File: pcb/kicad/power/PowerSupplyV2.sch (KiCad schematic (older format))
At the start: 61 parts, among them J1 12VWallWartVin, J2 AudioInput, J3 BackUpPower12V, J4 Display5V, J5 120Vinput, J7 Uc3.3VSignal, J8 Ucontroller3.3, U1 LM386, U11 BoostConv, U2 MOC3043M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

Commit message: Tile uC and antenna boards
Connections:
- wire segments 135 -> 141
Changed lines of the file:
@@
 	1    0    0    -1
 $EndComp
+Wire Wire Line
+	9750 4400 9750 4050
+Text Label 10200 3950 0    60   ~ 0
+5Voutput
 $Comp
 L CP C5
@@
 $EndComp
 Wire Wire Line
-	8900 3700 7950 3700
-Connection ~ 7950 3700
-Wire Wire Line
-	8450 3850 8450 3700
-Connection ~ 8450 3700
-Wire Wire Line
-	8750 3850 8750 3700
-Connection ~ 8750 3700
+	3350 2700 3350 2950
+Wire Wire Line
+	4800 2700 4800 3000
+Wire Wire Line
+	4250 3450 5500 3450
+Wire Wire Line
+	4800 3450 4800 3300
+Connection ~ 4800 3450
+Wire Wire Line
+	2700 3450 3950 3450
+Wire Wire Line
+	3350 3450 3350 3150
+Wire Wire Line
+	5050 3250 4950 3250
+Wire Wire Line
+	5350 3250 5500 3250
+Text Label 4850 2950 0    60   ~ 0
+MT2
+Text Label 4850 3400 0    60   ~ 0
+MT1
+Text Label 3350 2600 0    60   ~ 0
+ACLOAD
+Text Label 3300 3600 0    60   ~ 0
+ACNEUTRAL
 $Comp
 L R R12

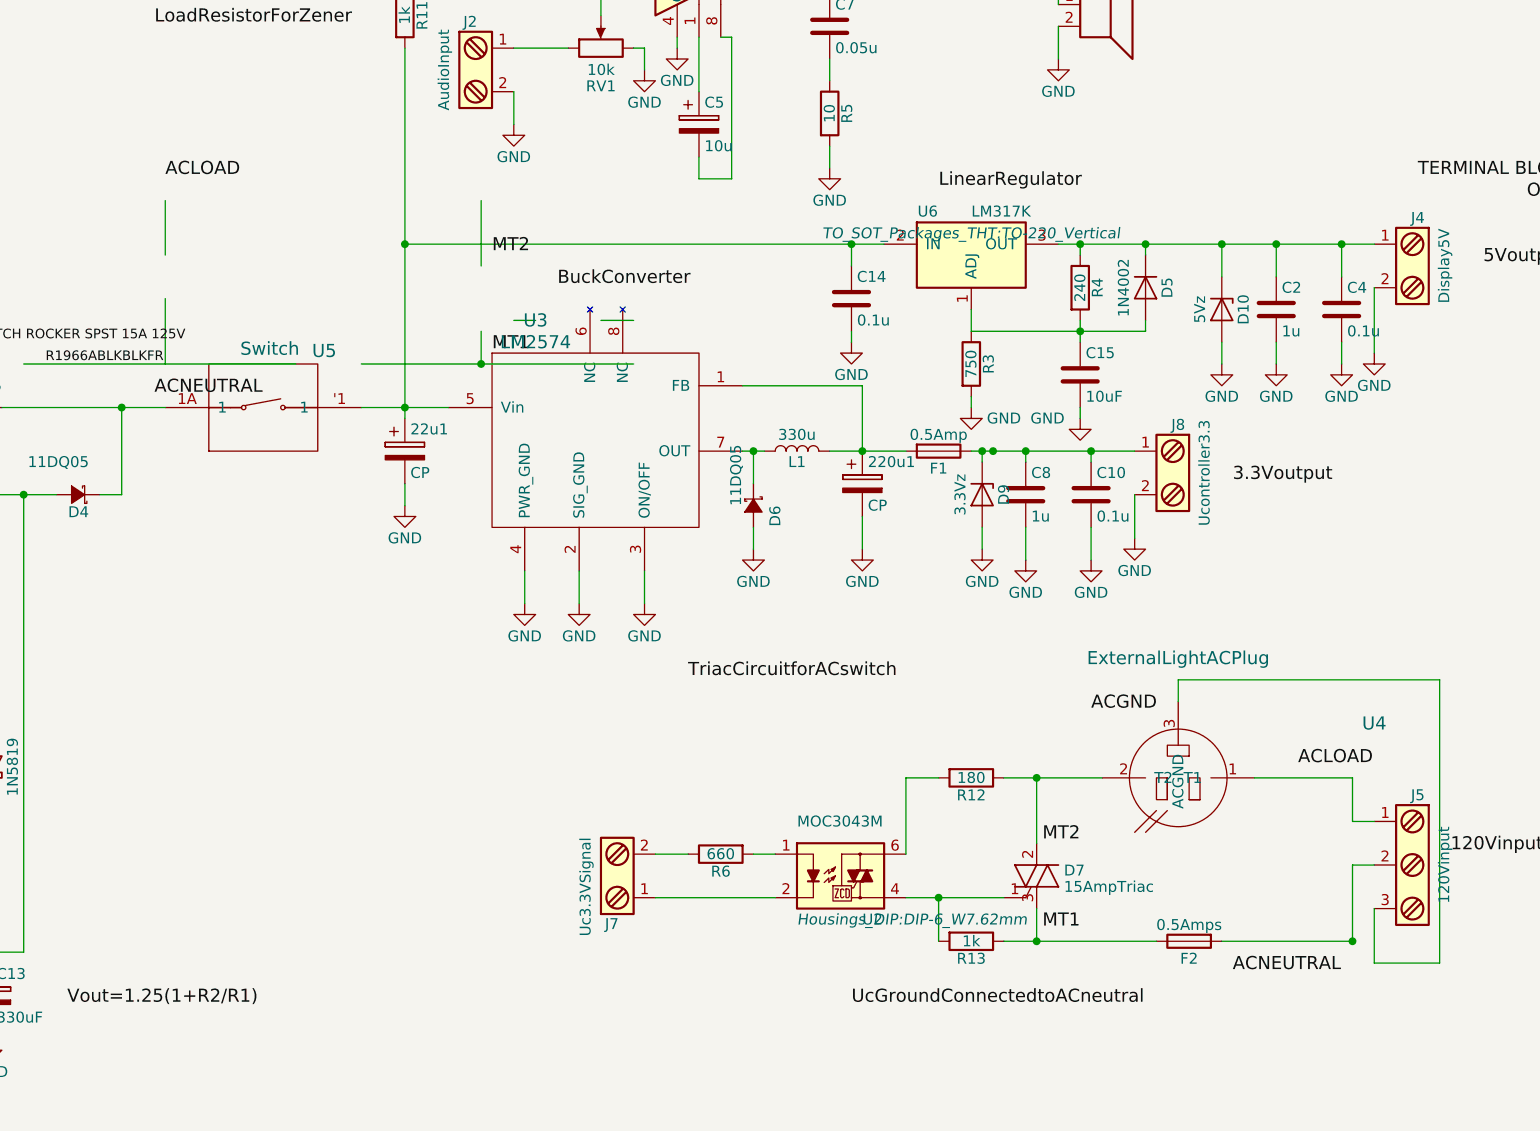
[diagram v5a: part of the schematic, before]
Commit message: Finish new base station and tile boards
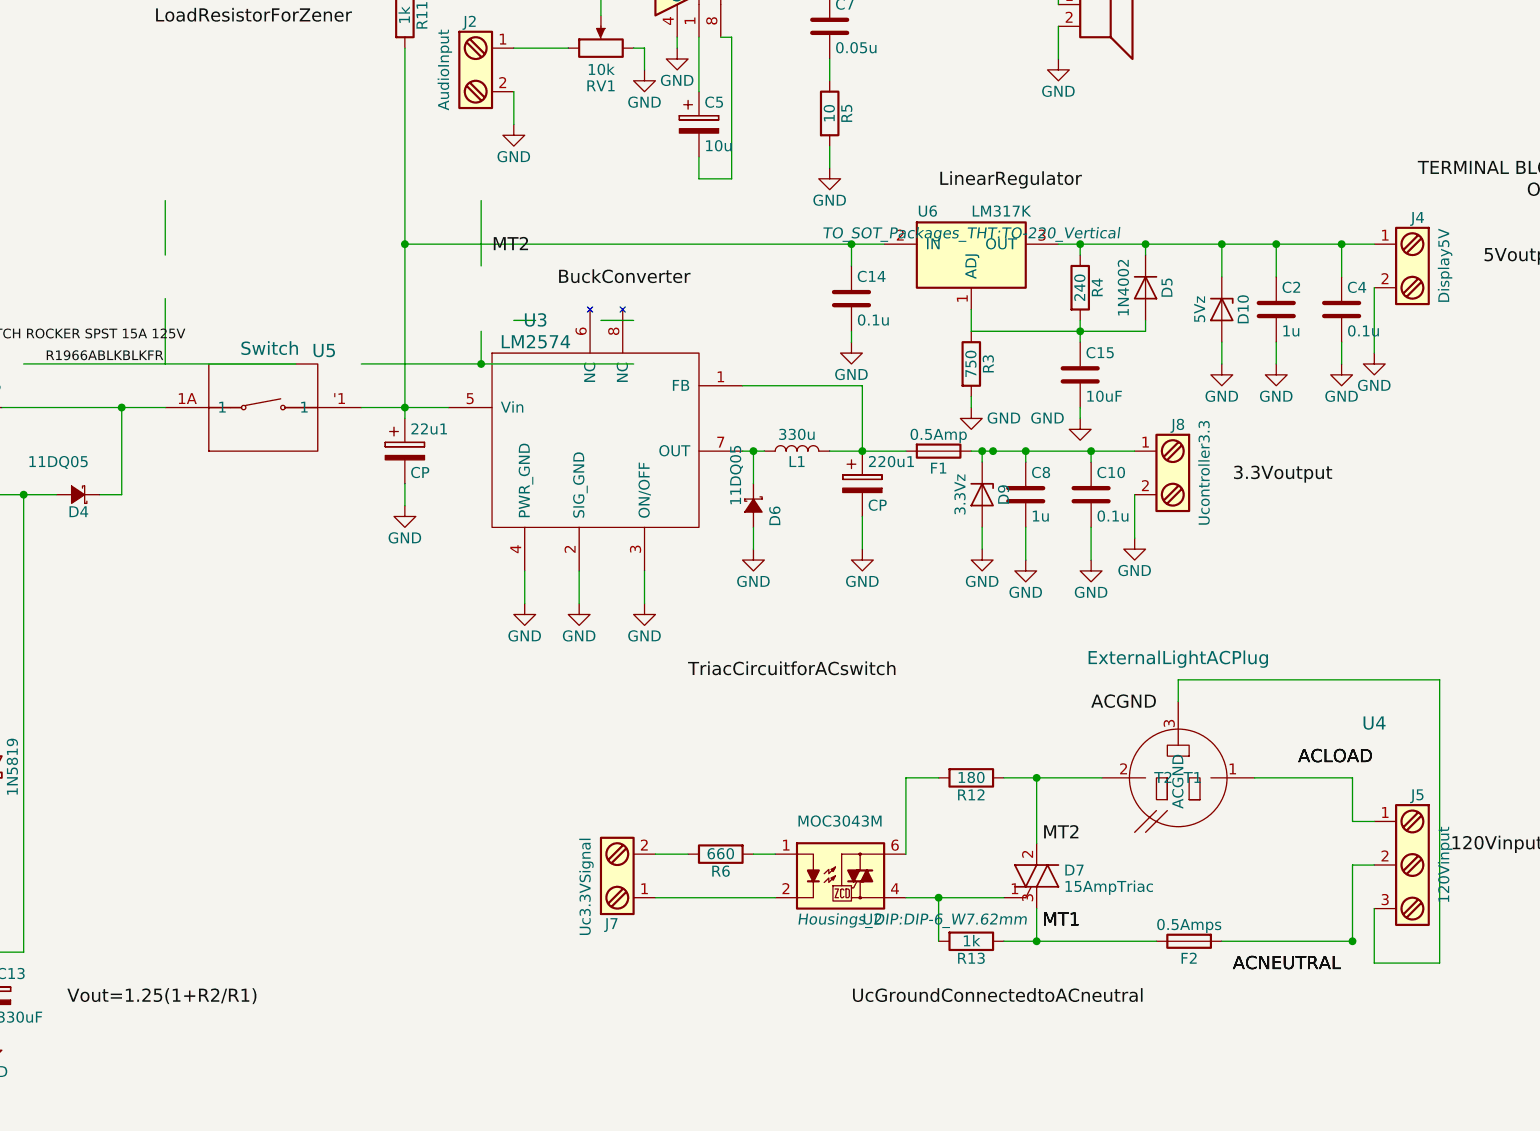
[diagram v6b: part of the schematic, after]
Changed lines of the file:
@@
 Text Label 4850 2950 0    60   ~ 0
 MT2
-Text Label 4850 3400 0    60   ~ 0
+Text Label 7550 6050 2    60   ~ 0
 MT1
-Text Label 3350 2600 0    60   ~ 0
+Text Label 8550 5300 0    60   ~ 0
 ACLOAD
-Text Label 3300 3600 0    60   ~ 0
+Text Label 8250 6250 0    60   ~ 0
 ACNEUTRAL
 $Comp
